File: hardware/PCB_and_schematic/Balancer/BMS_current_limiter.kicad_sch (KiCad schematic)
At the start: 34 parts, among them J21 BATT, J22 OUT, Q10 PMOS, Q11 BC327, Q12 BC337, Q22 BC817, Q23 BC817, Q24 BC337, Q25 BC327, Q9 PMOS

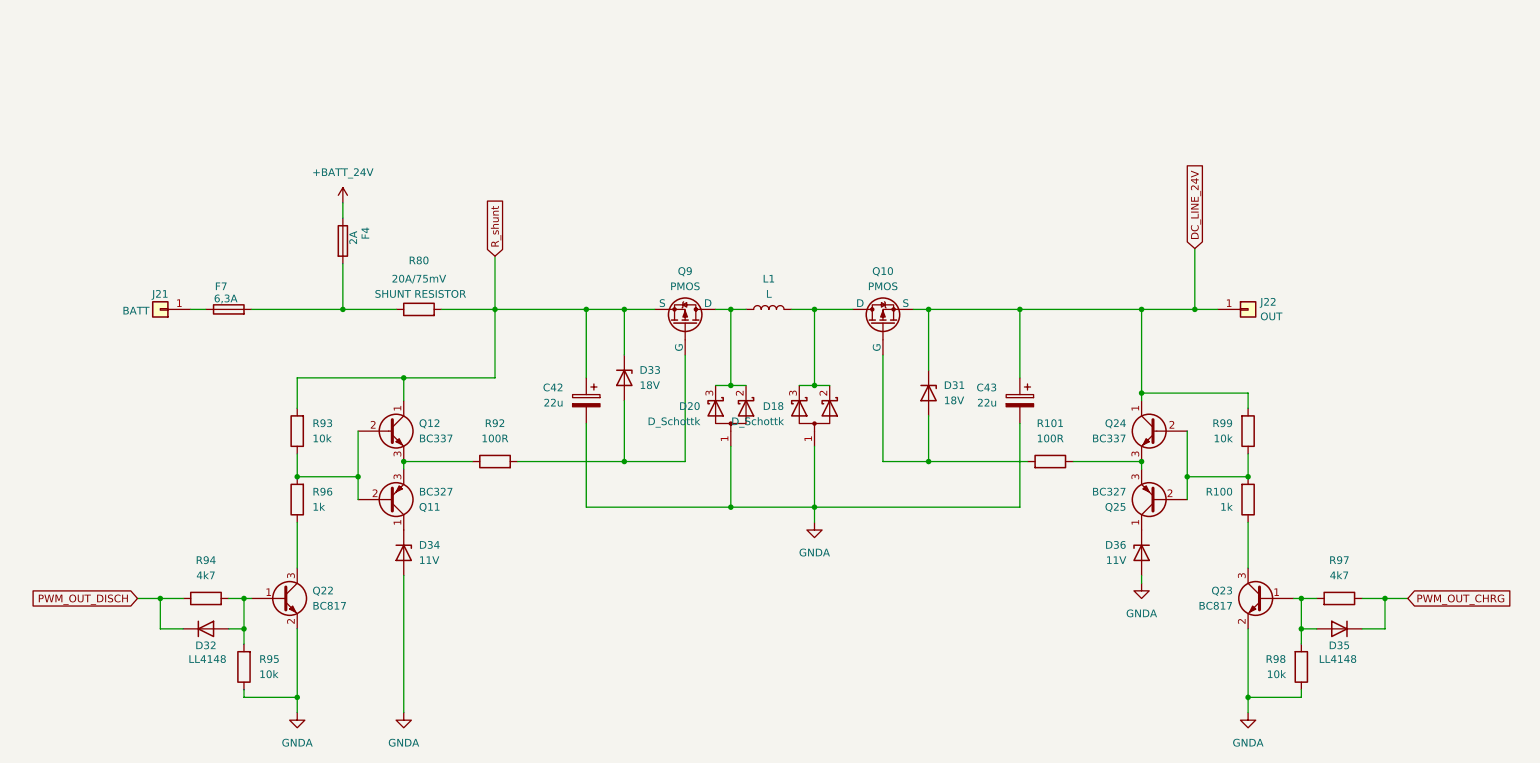
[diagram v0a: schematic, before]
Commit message: add simulations, split bms and esp schematics
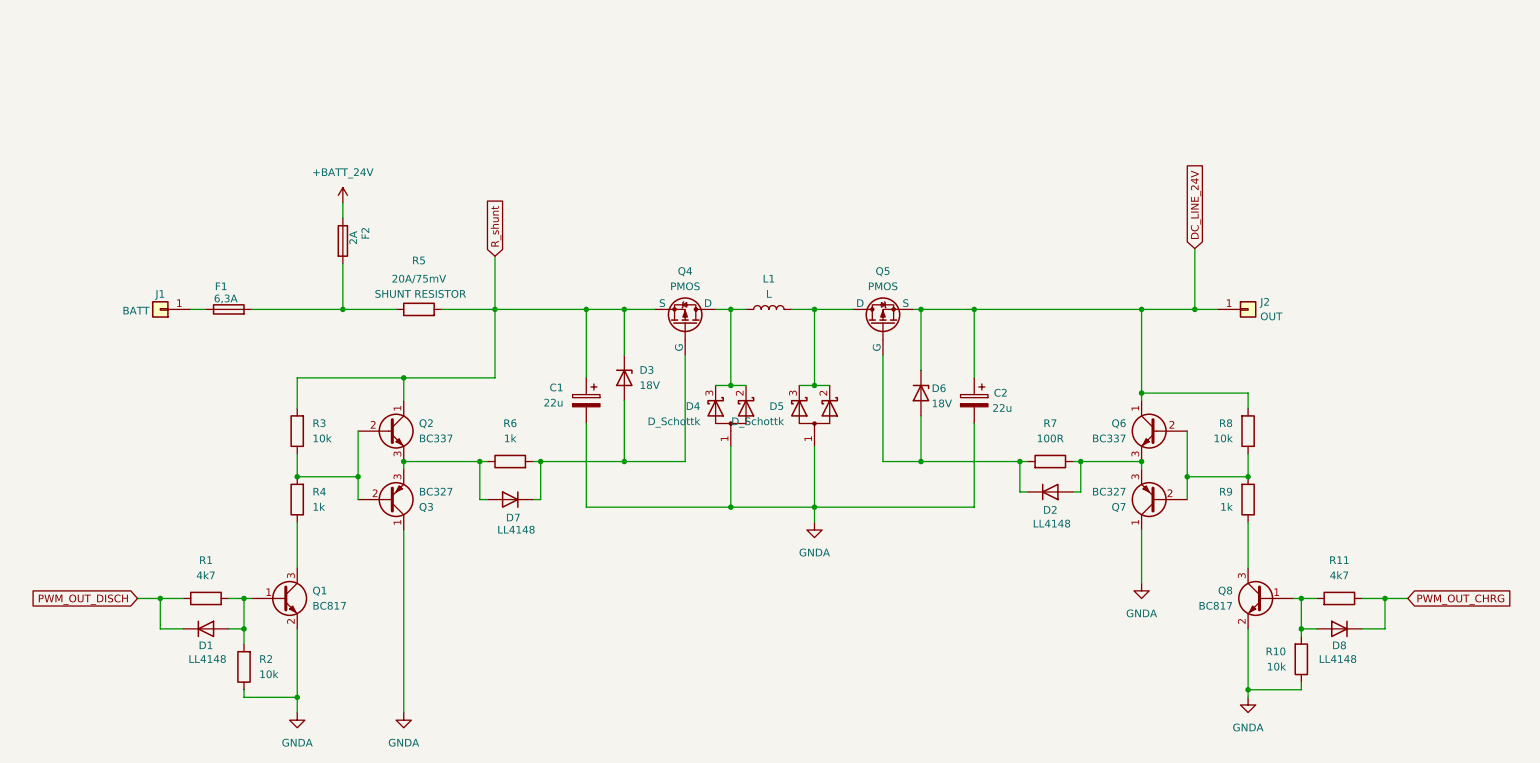
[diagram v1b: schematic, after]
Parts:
- removed D34, D36: 11V, symbol Device:D_Zener
- added D2, D7: LL4148, Diode_SMD:D_MiniMELF, symbol Diode:LL4148
- D3: renamed from D33; footprint (none) -> Diode_SMD:D_MiniMELF
- D4: renamed from D20; footprint (none) -> Package_TO_SOT_THT:TO-220-3_Vertical
- D5: renamed from D18; footprint (none) -> Package_TO_SOT_THT:TO-220-3_Vertical
- D6: renamed from D31; footprint (none) -> Diode_SMD:D_MiniMELF
- L1: footprint (none) -> Inductor_THT:L_Axial_L26.0mm_D11.0mm_P30.48mm_Horizontal_Fastron_77A
- Q4: renamed from Q9; footprint (none) -> Package_TO_SOT_THT:TO-220-3_Vertical
- Q5: renamed from Q10; footprint (none) -> Package_TO_SOT_THT:TO-220-3_Vertical
- R1: renamed from R94; footprint (none) -> Resistor_SMD:R_0805_2012Metric
- R10: renamed from R98; footprint (none) -> Resistor_SMD:R_0805_2012Metric
- R11: renamed from R97; footprint (none) -> Resistor_SMD:R_0805_2012Metric
- R2: renamed from R95; footprint (none) -> Resistor_SMD:R_0805_2012Metric
- R3: renamed from R93; footprint (none) -> Resistor_SMD:R_0805_2012Metric
- R4: renamed from R96; footprint (none) -> Resistor_SMD:R_0805_2012Metric
- R5: renamed from R80; footprint (none) -> Resistor_THT:R_Axial_Power_L38.0mm_W9.0mm_P40.64mm
- R6: renamed from R92; value 100R -> 1k; footprint (none) -> Resistor_SMD:R_0805_2012Metric
- R7: renamed from R101; footprint (none) -> Resistor_SMD:R_0805_2012Metric
- R8: renamed from R99; footprint (none) -> Resistor_SMD:R_0805_2012Metric
- R9: renamed from R100; footprint (none) -> Resistor_SMD:R_0805_2012Metric
- renumbered C42 to C1, C43 to C2, D32 to D1, D35 to D8, F7 to F1, F4 to F2, J21 to J1, J22 to J2, Q22 to Q1, Q12 to Q2, Q11 to Q3, Q24 to Q6, Q25 to Q7, Q23 to Q8
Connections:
- net GNDA: now also Q3.1 (C), Q7.1 (C)
- net at Q6.3 (E), Q7.3 (E), R7.1: now also D2.2 (A)
- net at D6.2 (A), Q5.2 (G), R7.2: now also D2.1 (K)
- net at Q2.3 (E), Q3.3 (E), R6.1: now also D7.2 (A)
- net at D3.2 (A), Q4.2 (G), R6.2: now also D7.1 (K)
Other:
- moved on the sheet: C2, D6, R10, R6

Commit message: Chceck and update DC module and meter probe pcb
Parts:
- F1, F2: footprint Fuse:Fuse_2512_6332Metric_Pad1.52x3.35mm_HandSolder -> Fuse:Fuseholder_Clip-5x20mm_Eaton_1A5601-01_Inline_P20.80x6.76mm_D1.70mm_Horizontal
- renumbered D7 to D2, D2 to D7
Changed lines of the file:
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@@
 		)
 		(instances
-			(project "Balancer+ESP"
+			(project "Balancer"
 				(path "/555ba40f-9abb-4b99-82c6-07e888fda9fd/f65ef685-3e95-4f8a-97fe-0688761539e6"
 					(reference "D4")
@@
 		)
 		(instances
-			(project "Balancer+ESP"
+			(project "Balancer"
 				(path "/555ba40f-9abb-4b99-82c6-07e888fda9fd/f65ef685-3e95-4f8a-97fe-0688761539e6"
 					(reference "R2")
@@
 		)
 		(instances
-			(project "Balancer+ESP"
+			(project "Balancer"
 				(path "/555ba40f-9abb-4b99-82c6-07e888fda9fd/f65ef685-3e95-4f8a-97fe-0688761539e6"
 					(reference "L1")
@@
 		)
 		(instances
-			(project "Balancer+ESP"
+			(project "Balancer"
 				(path "/555ba40f-9abb-4b99-82c6-07e888fda9fd/f65ef685-3e95-4f8a-97fe-0688761539e6"
 					(reference "Q7")
@@
 		)
 		(instances
-			(project "Balancer+ESP"
+			(project "Balancer"
 				(path "/555ba40f-9abb-4b99-82c6-07e888fda9fd/f65ef685-3e95-4f8a-97fe-0688761539e6"
 					(reference "R7")
@@
 		)
 		(instances
-			(project "Balancer+ESP"
+			(project "Balancer"
 				(path "/555ba40f-9abb-4b99-82c6-07e888fda9fd/f65ef685-3e95-4f8a-97fe-0688761539e6"
 					(reference "#PWR06")
@@
 		)
 		(instances
-			(project "Balancer+ESP"
+			(project "Balancer"
 				(path "/555ba40f-9abb-4b99-82c6-07e888fda9fd/f65ef685-3e95-4f8a-97fe-0688761539e6"
 					(reference "#PWR02")
@@
 		)
 		(instances
-			(project "Balancer+ESP"
+			(project "Balancer"
 				(path "/555ba40f-9abb-4b99-82c6-07e888fda9fd/f65ef685-3e95-4f8a-97fe-0688761539e6"
 					(reference "#PWR05")
@@
 		)
 		(instances
-			(project "Balancer+ESP"
+			(project "Balancer"
 				(path "/555ba40f-9abb-4b99-82c6-07e888fda9fd/f65ef685-3e95-4f8a-97fe-0688761539e6"
 					(reference "R4")
@@
 		)
 		(instances
-			(project "Balancer+ESP"
+			(project "Balancer"
 				(path "/555ba40f-9abb-4b99-82c6-07e888fda9fd/f65ef685-3e95-4f8a-97fe-0688761539e6"
 					(reference "R10")
@@
 		)
 		(instances
-			(project "Balancer+ESP"
+			(project "Balancer"
 				(path "/555ba40f-9abb-4b99-82c6-07e888fda9fd/f65ef685-3e95-4f8a-97fe-0688761539e6"
 					(reference "C1")
@@
 		)
 		(instances
-			(project "Balancer+ESP"
+			(project "Balancer"
 				(path "/555ba40f-9abb-4b99-82c6-07e888fda9fd/f65ef685-3e95-4f8a-97fe-0688761539e6"
 					(reference "D6")
@@
 		)
 		(instances
-			(project "Balancer+ESP"
+			(project "Balancer"
 				(path "/555ba40f-9abb-4b99-82c6-07e888fda9fd/f65ef685-3e95-4f8a-97fe-0688761539e6"
 					(reference "Q5")
@@
 		)
 		(instances
-			(project "Balancer+ESP"
+			(project "Balancer"
 				(path "/555ba40f-9abb-4b99-82c6-07e888fda9fd/f65ef685-3e95-4f8a-97fe-0688761539e6"
 					(reference "Q3")
@@
 		)
 		(instances
-			(project "Balancer+ESP"
+			(project "Balancer"
 				(path "/555ba40f-9abb-4b99-82c6-07e888fda9fd/f65ef685-3e95-4f8a-97fe-0688761539e6"
 					(reference "R5")
@@
 			)
 		)
-		(property "Footprint" "Fuse:Fuse_2512_6332Metric_Pad1.52x3.35mm_HandSolder"
+		(property "Footprint" "Fuse:Fuseholder_Clip-5x20mm_Eaton_1A5601-01_Inline_P20.80x6.76mm_D1.70mm_Horizontal"
 			(at 83.312 45.72 90)
 			(effects
@@
 		)
 		(instances
-			(project "Balancer+ESP"
+			(project "Balancer"
 				(path "/555ba40f-9abb-4b99-82c6-07e888fda9fd/f65ef685-3e95-4f8a-97fe-0688761539e6"
 					(reference "F2")
@@
 		)
 		(instances
-			(project "Balancer+ESP"
+			(project "Balancer"
 				(path "/555ba40f-9abb-4b99-82c6-07e888fda9fd/f65ef685-3e95-4f8a-97fe-0688761539e6"
 					(reference "C2")
@@
 		)
 		(instances
-			(project "Balancer+ESP"
+			(project "Balancer"
 				(path "/555ba40f-9abb-4b99-82c6-07e888fda9fd/f65ef685-3e95-4f8a-97fe-0688761539e6"
 					(reference "R8")
@@
 		(on_board yes)
 		(dnp no)
-		(property "Reference" "D7"
+		(property "Reference" "D2"
 			(at 113.538 91.948 0)
 			(effects
@@
 		)
 		(instances
-			(project "Balancer+ESP"
-				(path "/555ba40f-9abb-4b99-82c6-07e888fda9fd/f65ef685-3e95-4f8a-97fe-0688761539e6"
-					(reference "D7")
+			(project "Balancer"
+				(path "/555ba40f-9abb-4b99-82c6-07e888fda9fd/f65ef685-3e95-4f8a-97fe-0688761539e6"
+					(reference "D2")
 					(unit 1)
 				)
@@
 		)
 		(instances
-			(project "Balancer+ESP"
+			(project "Balancer"
 				(path "/555ba40f-9abb-4b99-82c6-07e888fda9fd/f65ef685-3e95-4f8a-97fe-0688761539e6"
 					(reference "Q2")
@@
 			)
 		)
-		(property "Footprint" "Fuse:Fuse_2512_6332Metric_Pad1.52x3.35mm_HandSolder"
+		(property "Footprint" "Fuse:Fuseholder_Clip-5x20mm_Eaton_1A5601-01_Inline_P20.80x6.76mm_D1.70mm_Horizontal"
 			(at 66.04 58.928 90)
 			(effects
@@
 		)
 		(instances
-			(project "Balancer+ESP"
+			(project "Balancer"
 				(path "/555ba40f-9abb-4b99-82c6-07e888fda9fd/f65ef685-3e95-4f8a-97fe-0688761539e6"
 					(reference "F1")
@@
 		)
 		(instances
-			(project "Balancer+ESP"
+			(project "Balancer"
 				(path "/555ba40f-9abb-4b99-82c6-07e888fda9fd/f65ef685-3e95-4f8a-97fe-0688761539e6"
 					(reference "D1")
@@
 		(on_board yes)
 		(dnp no)
-		(property "Reference" "D2"
+		(property "Reference" "D7"
 			(at 203.2 90.678 0)
 			(effects
@@
 		)
 		(instances
-			(project "Balancer+ESP"
-				(path "/555ba40f-9abb-4b99-82c6-07e888fda9fd/f65ef685-3e95-4f8a-97fe-0688761539e6"
-					(reference "D2")
+			(project "Balancer"
+				(path "/555ba40f-9abb-4b99-82c6-07e888fda9fd/f65ef685-3e95-4f8a-97fe-0688761539e6"
+					(reference "D7")
 					(unit 1)
 				)
@@
 		)
 		(instances
-			(project "Balancer+ESP"
+			(project "Balancer"
 				(path "/555ba40f-9abb-4b99-82c6-07e888fda9fd/f65ef685-3e95-4f8a-97fe-0688761539e6"
 					(reference "Q8")
@@
 		)
 		(instances
-			(project "Balancer+ESP"
+			(project "Balancer"
 				(path "/555ba40f-9abb-4b99-82c6-07e888fda9fd/f65ef685-3e95-4f8a-97fe-0688761539e6"
 					(reference "#PWR01")
@@
 		)
 		(instances
-			(project "Balancer+ESP"
+			(project "Balancer"
 				(path "/555ba40f-9abb-4b99-82c6-07e888fda9fd/f65ef685-3e95-4f8a-97fe-0688761539e6"
 					(reference "Q4")
@@
 		)
 		(instances
-			(project "Balancer+ESP"
+			(project "Balancer"
 				(path "/555ba40f-9abb-4b99-82c6-07e888fda9fd/f65ef685-3e95-4f8a-97fe-0688761539e6"
 					(reference "#PWR03")
@@
 		)
 		(instances
-			(project "Balancer+ESP"
+			(project "Balancer"
 				(path "/555ba40f-9abb-4b99-82c6-07e888fda9fd/f65ef685-3e95-4f8a-97fe-0688761539e6"
 					(reference "R6")
@@
 		)
 		(instances
-			(project "Balancer+ESP"
+			(project "Balancer"
 				(path "/555ba40f-9abb-4b99-82c6-07e888fda9fd/f65ef685-3e95-4f8a-97fe-0688761539e6"
 					(reference "Q1")
@@
 		)
 		(instances
-			(project "Balancer+ESP"
+			(project "Balancer"
 				(path "/555ba40f-9abb-4b99-82c6-07e888fda9fd/f65ef685-3e95-4f8a-97fe-0688761539e6"
 					(reference "Q6")
@@
 		)
 		(instances
-			(project "Balancer+ESP"
+			(project "Balancer"
 				(path "/555ba40f-9abb-4b99-82c6-07e888fda9fd/f65ef685-3e95-4f8a-97fe-0688761539e6"
 					(reference "J1")
@@
 		)
 		(instances
-			(project "Balancer+ESP"
+			(project "Balancer"
 				(path "/555ba40f-9abb-4b99-82c6-07e888fda9fd/f65ef685-3e95-4f8a-97fe-0688761539e6"
 					(reference "D5")
@@
 		)
 		(instances
-			(project "Balancer+ESP"
+			(project "Balancer"
 				(path "/555ba40f-9abb-4b99-82c6-07e888fda9fd/f65ef685-3e95-4f8a-97fe-0688761539e6"
 					(reference "#PWR04")
@@
 		)
 		(instances
-			(project "Balancer+ESP"
+			(project "Balancer"
 				(path "/555ba40f-9abb-4b99-82c6-07e888fda9fd/f65ef685-3e95-4f8a-97fe-0688761539e6"
 					(reference "D3")
@@
 		)
 		(instances
-			(project "Balancer+ESP"
+			(project "Balancer"
 				(path "/555ba40f-9abb-4b99-82c6-07e888fda9fd/f65ef685-3e95-4f8a-97fe-0688761539e6"
 					(reference "R1")
@@
 		)
 		(instances
-			(project "Balancer+ESP"
+			(project "Balancer"
 				(path "/555ba40f-9abb-4b99-82c6-07e888fda9fd/f65ef685-3e95-4f8a-97fe-0688761539e6"
 					(reference "R11")
@@
 		)
 		(instances
-			(project "Balancer+ESP"
+			(project "Balancer"
 				(path "/555ba40f-9abb-4b99-82c6-07e888fda9fd/f65ef685-3e95-4f8a-97fe-0688761539e6"
 					(reference "R3")
@@
 		)
 		(instances
-			(project "Balancer+ESP"
+			(project "Balancer"
 				(path "/555ba40f-9abb-4b99-82c6-07e888fda9fd/f65ef685-3e95-4f8a-97fe-0688761539e6"
 					(reference "D8")
@@
 		)
 		(instances
-			(project "Balancer+ESP"
+			(project "Balancer"
 				(path "/555ba40f-9abb-4b99-82c6-07e888fda9fd/f65ef685-3e95-4f8a-97fe-0688761539e6"
 					(reference "R9")
@@
 		)
 		(instances
-			(project "Balancer+ESP"
+			(project "Balancer"
 				(path "/555ba40f-9abb-4b99-82c6-07e888fda9fd/f65ef685-3e95-4f8a-97fe-0688761539e6"
 					(reference "J2")

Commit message: part placement of bms pcb
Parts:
- F1, F2: footprint Fuse:Fuseholder_Clip-5x20mm_Eaton_1A5601-01_Inline_P20.80x6.76mm_D1.70mm_Horizontal -> Fuse:Fuse_Blade_ATO_directSolder
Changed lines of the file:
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@@
 			)
 		)
-		(property "Footprint" "Fuse:Fuseholder_Clip-5x20mm_Eaton_1A5601-01_Inline_P20.80x6.76mm_D1.70mm_Horizontal"
+		(property "Footprint" "Fuse:Fuse_Blade_ATO_directSolder"
 			(at 83.312 45.72 90)
 			(effects
@@
 			)
 		)
-		(property "Footprint" "Fuse:Fuseholder_Clip-5x20mm_Eaton_1A5601-01_Inline_P20.80x6.76mm_D1.70mm_Horizontal"
+		(property "Footprint" "Fuse:Fuse_Blade_ATO_directSolder"
 			(at 66.04 58.928 90)
 			(effects

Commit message: Routing balancer pcb
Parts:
- D4, D5, Q4, Q5: footprint Package_TO_SOT_THT:TO-220-3_Vertical -> My-Footprints:TO-220-3_V_Thick_Pads
- Q2, Q3, Q6, Q7: footprint Package_TO_SOT_THT:TO-92_Inline -> My-Footprints:TO-92_Inline_Wide
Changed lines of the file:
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@@
 			)
 		)
-		(property "Footprint" "Package_TO_SOT_THT:TO-220-3_Vertical"
+		(property "Footprint" "My-Footprints:TO-220-3_V_Thick_Pads"
 			(at 149.86 76.2 0)
 			(effects
@@
 			)
 		)
-		(property "Footprint" "Package_TO_SOT_THT:TO-92_Inline"
+		(property "Footprint" "My-Footprints:TO-92_Inline_Wide"
 			(at 215.9 86.995 0)
 			(effects
@@
 			)
 		)
-		(property "Footprint" "Package_TO_SOT_THT:TO-220-3_Vertical"
+		(property "Footprint" "My-Footprints:TO-220-3_V_Thick_Pads"
 			(at 172.72 54.61 0)
 			(effects
@@
 			)
 		)
-		(property "Footprint" "Package_TO_SOT_THT:TO-92_Inline"
+		(property "Footprint" "My-Footprints:TO-92_Inline_Wide"
 			(at 97.79 86.995 0)
 			(effects
@@
 			)
 		)
-		(property "Footprint" "Package_TO_SOT_THT:TO-92_Inline"
+		(property "Footprint" "My-Footprints:TO-92_Inline_Wide"
 			(at 97.79 79.375 0)
 			(effects
@@
 			)
 		)
-		(property "Footprint" "Package_TO_SOT_THT:TO-220-3_Vertical"
+		(property "Footprint" "My-Footprints:TO-220-3_V_Thick_Pads"
 			(at 144.78 54.61 0)
 			(effects
@@
 			)
 		)
-		(property "Footprint" "Package_TO_SOT_THT:TO-92_Inline"
+		(property "Footprint" "My-Footprints:TO-92_Inline_Wide"
 			(at 215.9 79.375 0)
 			(effects
@@
 			)
 		)
-		(property "Footprint" "Package_TO_SOT_THT:TO-220-3_Vertical"
+		(property "Footprint" "My-Footprints:TO-220-3_V_Thick_Pads"
 			(at 163.83 76.2 0)
 			(effects

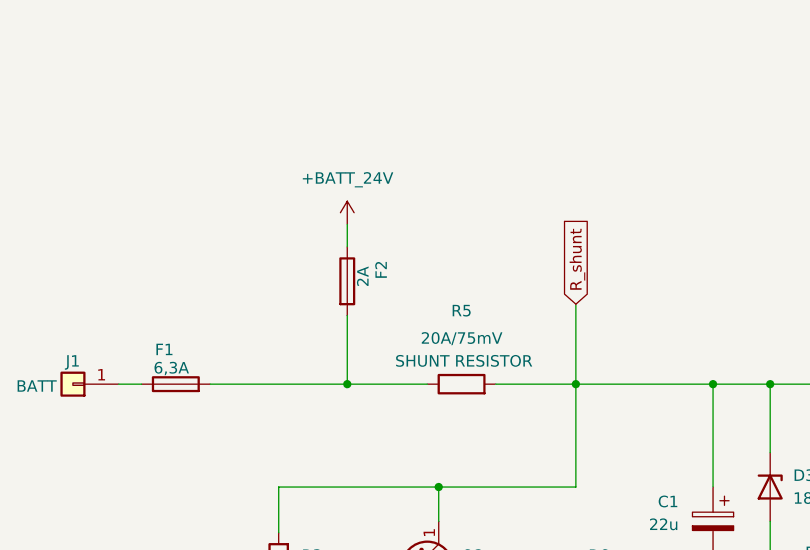
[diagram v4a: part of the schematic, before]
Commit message: Splitter and connector footprints, progress with balancer pcb routing
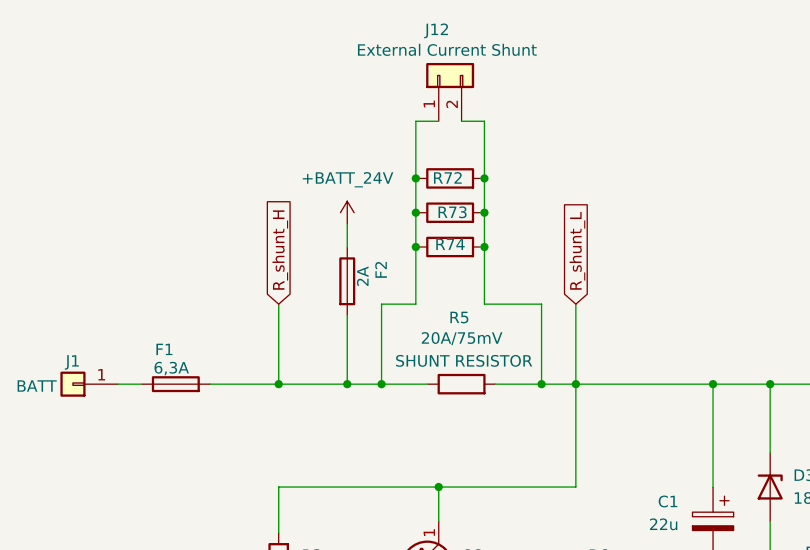
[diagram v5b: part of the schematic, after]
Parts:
- added J12: External Current Shunt, Connector_Hirose:Hirose_DF63M-2P-3.96DSA_1x02_P3.96mm_Vertical, symbol Connector_Generic:Conn_01x02
- added R72, R73: 20A/75mV, Resistor_THT:R_Axial_DIN0309_L9.0mm_D3.2mm_P20.32mm_Horizontal, symbol Device:R
- added R74: R, Resistor_THT:R_Axial_DIN0309_L9.0mm_D3.2mm_P20.32mm_Horizontal, symbol Device:R
- R5: footprint Resistor_THT:R_Axial_Power_L38.0mm_W9.0mm_P40.64mm -> My-Footprints:Resistor-Power-5W-L22-W10
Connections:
- net R_shunt_H: now reaches F1.2, F2.2, R5.1
- net R_shunt_H: now also J12.1 (Pin_1), R72.1, R73.1, R74.1
- net R_shunt renamed R_shunt_L
- net R_shunt_L: now also J12.2 (Pin_2), R72.2, R73.2, R74.2
